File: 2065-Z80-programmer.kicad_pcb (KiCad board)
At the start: 2 copper layers, 100 x 65 mm, 31 parts, among them J1 Conn_01x05, J2 Conn_02x20_Counter_Clockwise, J3 Conn_01x02, J4 Conn_02x20_Odd_Even, Q1 2N7000, Q2 2N7000, Q3 PN2222, U1 MCP23017-E_SP, U2 MCP23017-E_SP

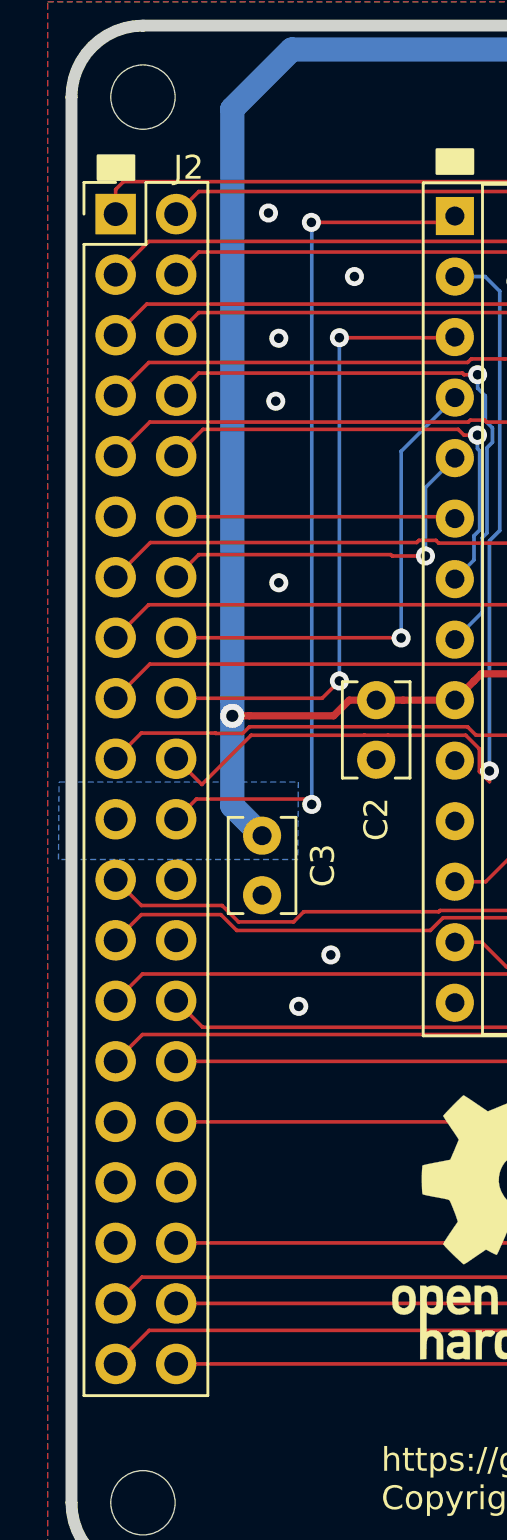
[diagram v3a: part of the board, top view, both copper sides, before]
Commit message: Change Z80 header to socket so looks right in 3D
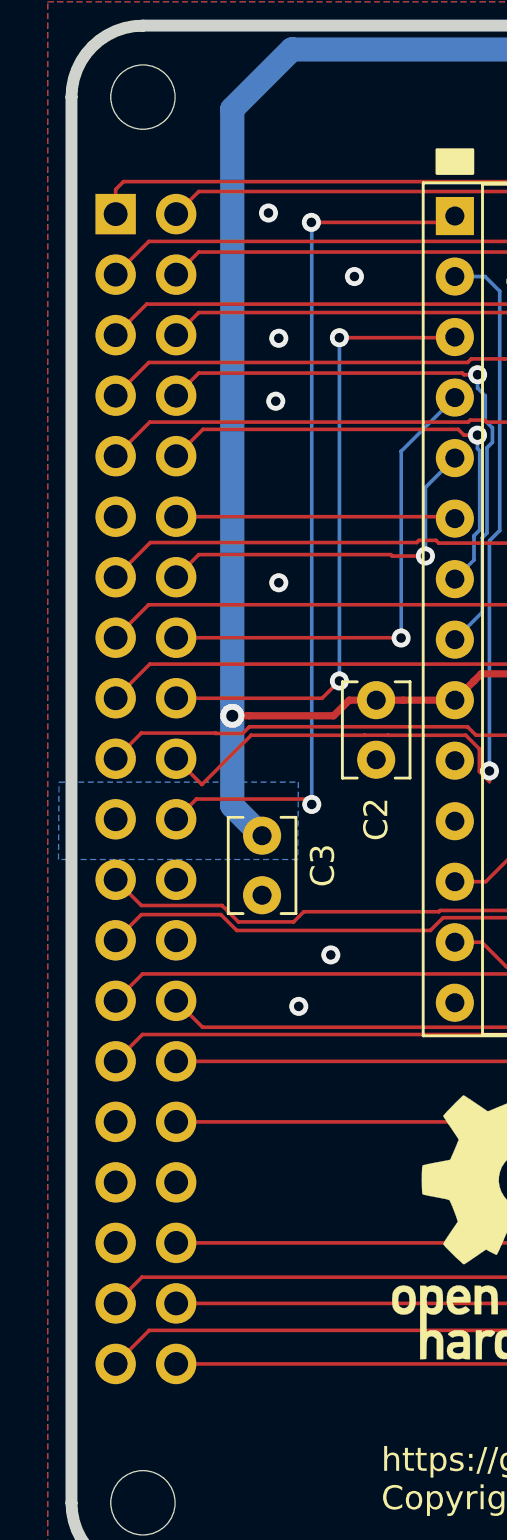
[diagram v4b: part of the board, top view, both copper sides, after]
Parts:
- J2: footprint jb-footprint:PinHeader_2x20_P2.54mm_Vertical_counterclock -> jb-footprint:PinSocket_2x20_P2.54mm_Vertical_clockwise; moved to B.Cu
- R1, R2, R3, R4: value 2K2 -> 2K7
- turned J2 to 180 degrees

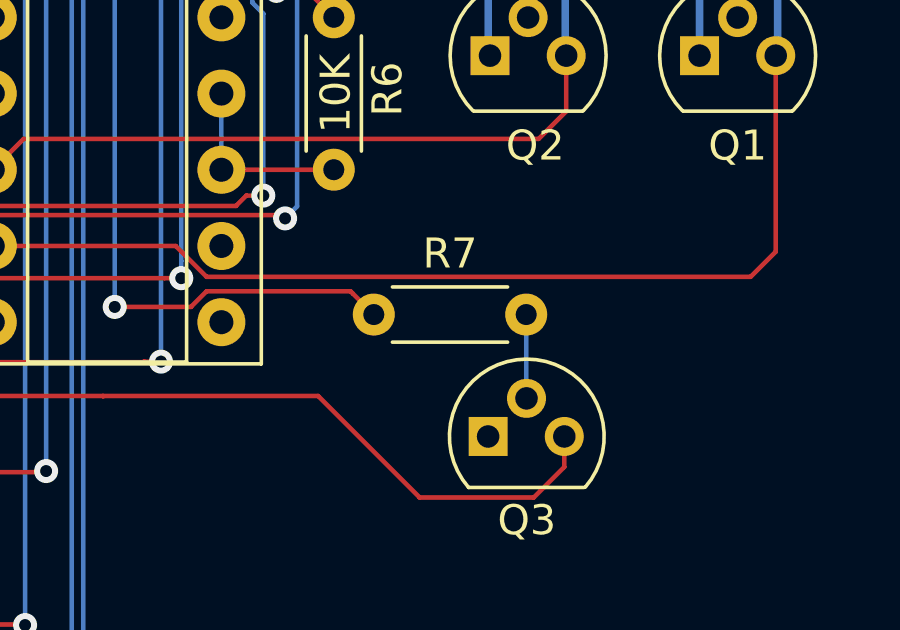
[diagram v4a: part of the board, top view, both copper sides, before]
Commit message: Add 1K value to silkscreen for R7
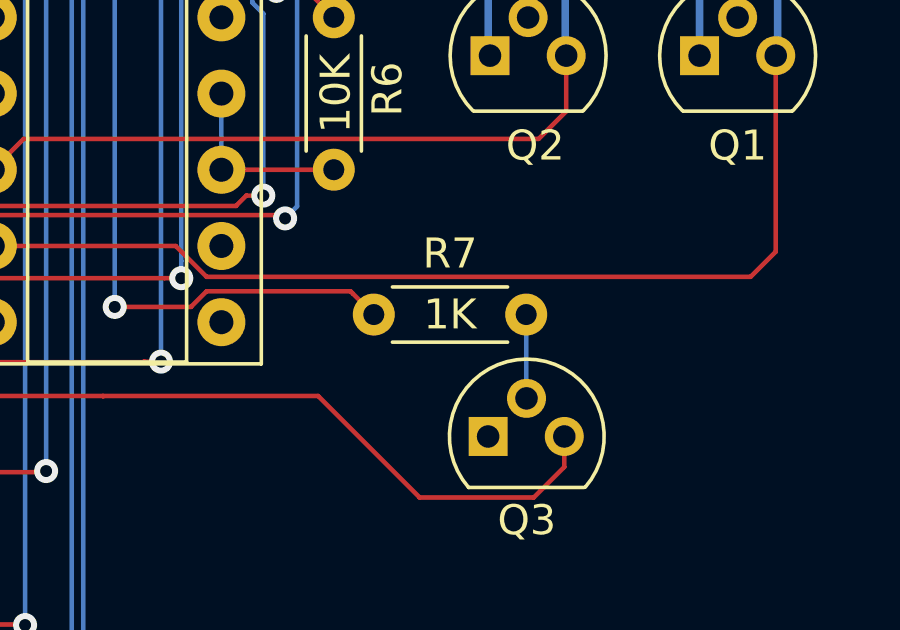
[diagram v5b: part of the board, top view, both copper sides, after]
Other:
- board text added: "1K"
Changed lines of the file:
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@@
   (general
     (thickness 1.6)
-    (drawings 35)
+    (drawings 36)
     (tracks 490)
     (zones 0)
@@
     )
   )
+  (gr_text 1K (at 138.684 95.758) (layer F.SilkS)
+    (effects (font (size 1 1) (thickness 0.15)))
+  )
   (gr_text 10K (at 111.506 88.392 90) (layer F.SilkS)

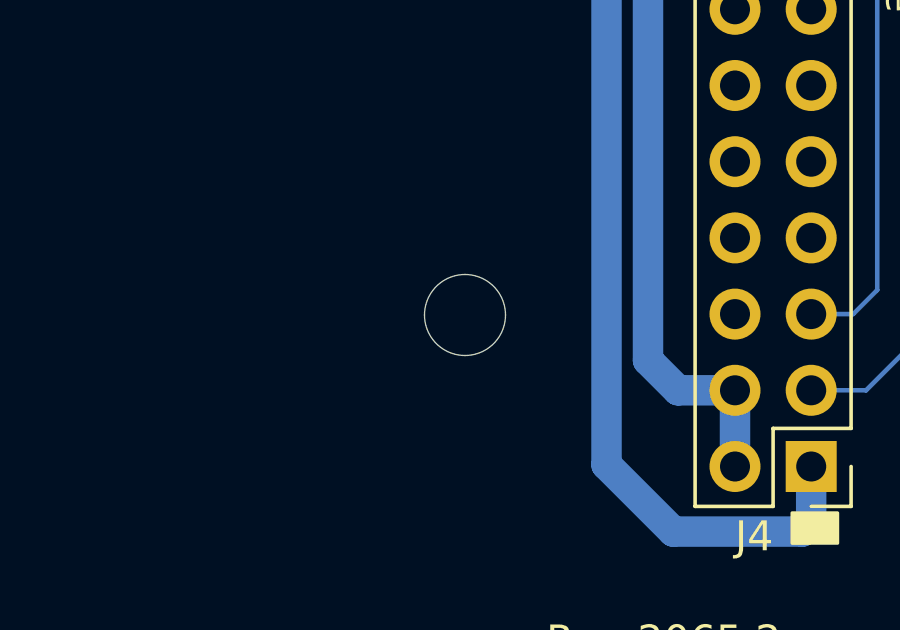
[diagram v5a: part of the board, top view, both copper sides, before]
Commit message: Move H5 1mm to the left & ignore scratch files.
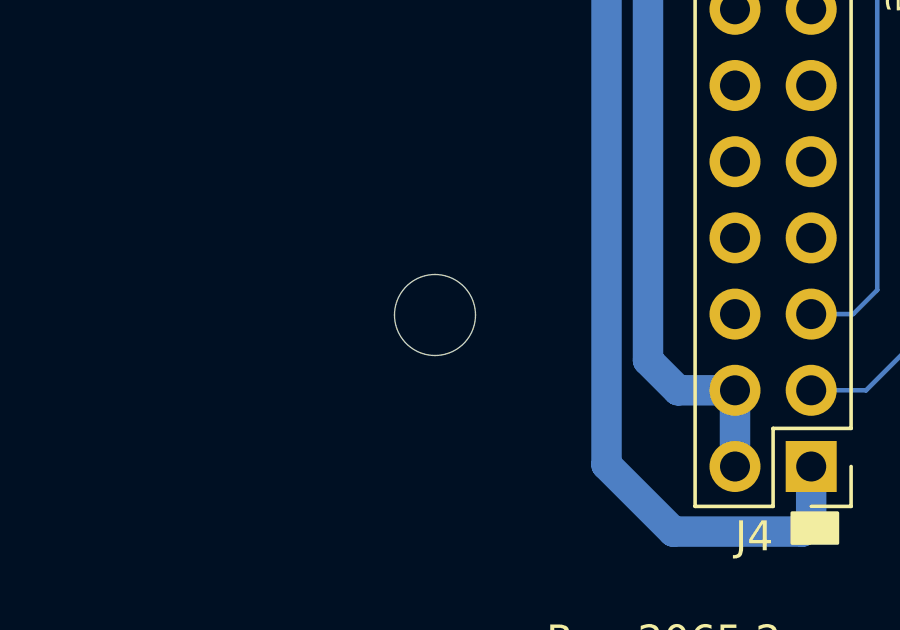
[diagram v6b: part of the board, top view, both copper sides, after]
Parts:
- moved H5 1.00 mm to (163.0, 107.2)
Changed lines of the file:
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@@
   )
   (module MountingHole:MountingHole_2.7mm_M2.5_DIN965 (layer F.Cu)
-    (at 164 107.19)
+    (at 163 107.19)
     (descr "Mounting Hole 2.7mm, no annular, M2.5, DIN965")
     (tags "mounting hole 2.7mm no annular m2.5 din965")
